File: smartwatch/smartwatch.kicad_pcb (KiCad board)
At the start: 2 copper layers, 40.1 x 40.1 mm, 2 parts, among them U1 ESP32-S3-WROOM-1, U2 AMS1117-3.3

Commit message: finished pcb and sch
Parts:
- added BOOT/FLASH1: BOOT/FLASH, Button_Switch_SMD:SW_SPST_Omron_B3FS-100xP, B.Cu at (72.2, 53.5)
- added C1: 10nF, Capacitor_SMD:C_0805_2012Metric_Pad1.18x1.45mm_HandSolder, B.Cu at (49.6, 71.7)
- added C10: 100nF, Capacitor_SMD:C_0805_2012Metric_Pad1.18x1.45mm_HandSolder, B.Cu at (58.2, 48.6)
- added C11: Polarized_10uF, Capacitor_Tantalum_SMD:CP_EIA-2012-12_Kemet-R_Pad1.30x1.05mm_HandSolder, B.Cu at (67.3, 71.8)
- added C12: Polarized_10uF, Capacitor_Tantalum_SMD:CP_EIA-2012-12_Kemet-R_Pad1.30x1.05mm_HandSolder, B.Cu at (57.1, 74.1)
- added C2: 100nF, Capacitor_SMD:C_0805_2012Metric_Pad1.18x1.45mm_HandSolder, B.Cu at (53.7, 71.6)
- added C3: 100nF, Capacitor_SMD:C_0805_2012Metric_Pad1.18x1.45mm_HandSolder, B.Cu at (44.8, 67.6)
- added C4: 10nF, Capacitor_SMD:C_0805_2012Metric_Pad1.18x1.45mm_HandSolder, B.Cu at (44.7, 64.3)
- added C5: 0.1uF, Capacitor_SMD:C_0805_2012Metric_Pad1.18x1.45mm_HandSolder, F.Cu at (45.6, 60.3)
- added C6: 2.2nF, Capacitor_SMD:C_0805_2012Metric_Pad1.18x1.45mm_HandSolder, F.Cu at (46.2, 52.3)
- added C7: 0.1uF, Capacitor_SMD:C_0805_2012Metric_Pad1.18x1.45mm_HandSolder, F.Cu at (41.7, 60.8)
- added C8: 10nF, Capacitor_SMD:C_0805_2012Metric_Pad1.18x1.45mm_HandSolder, F.Cu at (39.6, 56.6)
- added C9: 100nF, Capacitor_SMD:C_0805_2012Metric_Pad1.18x1.45mm_HandSolder, B.Cu at (72.2, 47.5)
- added GREEN1: CHARGED, LED_SMD:LED_0805_2012Metric_Pad1.15x1.40mm_HandSolder, B.Cu at (68.2, 60.2)
- added J1: BAT_CON, Connector_Wire_SMD:Wire_Pad_1x02, B.Cu at (64.1, 74.0)
- added J2: DC_CON, Connector_Wire_SMD:Wire_Pad_1x02, B.Cu at (59.6, 74.7)
- added J3: PROG_INT, Connector_Wire_SMD:Wire_Pad_1x02, F.Cu at (70.3, 52.3)
- added J4: I2C Touch, Connector_Wire_SMD:Wire_Pad_1x02, F.Cu at (75.4, 52.3)
- added J5: SPI Display, Connector_Wire_SMD:Wire_Pad_1x03, F.Cu at (70.1, 57.1)
- added J6: Power, Connector_Wire_SMD:Wire_Pad_1x02, B.Cu at (71.6, 67.6)
- added J7: Micro_SD_Card, Connector_Card:microSD_HC_Hirose_DM3D-SF, B.Cu at (49.3, 54.1)
- added R1: 2.2KΩ, Resistor_SMD:R_0805_2012Metric_Pad1.20x1.40mm_HandSolder, B.Cu at (63.6, 68.0)
- added R2: 470Ω, Resistor_SMD:R_0805_2012Metric_Pad1.20x1.40mm_HandSolder, B.Cu at (59.6, 60.3)
- added R3: 470Ω, Resistor_SMD:R_0805_2012Metric_Pad1.20x1.40mm_HandSolder, B.Cu at (68.0, 62.9)
- added RED1: CHARGING, LED_SMD:LED_0805_2012Metric_Pad1.15x1.40mm_HandSolder, B.Cu at (63.5, 60.3)
- added RST1: RST, Button_Switch_SMD:SW_SPST_Omron_B3FS-100xP, B.Cu at (61.8, 53.5)
- added U3: MPU-6050, Sensor_Motion:InvenSense_QFN-24_4x4mm_P0.5mm, F.Cu at (43.3, 56.2)
- added U4: TLV1117-33, Package_TO_SOT_SMD:SOT-223-3_TabPin2, B.Cu at (51.5, 66.3)
- U1: value ESP32-S3-WROOM-1 -> ESP32-WROVER-E
- U2: value AMS1117-3.3 -> MCP73831-5-OT; footprint Package_TO_SOT_SMD:SOT-223-3_TabPin2 -> Package_TO_SOT_SMD:SOT-23-5; moved to B.Cu
- moved U2 18.6 mm to (59.5, 68.1), turned to 180 degrees
- moved U1 0.29 mm to (58.6, 56.2)
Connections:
- U1 pad 1: Net-(U1-GND-Pad1) -> DC_GND
- U1 pad 13: unconnected-(U1-GPIO19/U1RTS/ADC2_CH8/CLK_OUT2/USB_D--Pad13) -> SD_SCLK
- U1 pad 14: unconnected-(U1-GPIO20/U1CTS/ADC2_CH9/CLK_OUT1/USB_D+-Pad14) -> SD_MISO
- U1 pad 15: unconnected-(U1-GPIO3/TOUCH3/ADC1_CH2-Pad15) -> DC_GND
- U1 pad 16: unconnected-(U1-GPIO46-Pad16) -> SD_MOSI
- U1 pad 17: unconnected-(U1-GPIO9/TOUCH9/ADC1_CH8/FSPIHD/SUBSPIHD-Pad17) -> (no net)
- U1 pad 18: unconnected-(U1-GPIO10/TOUCH10/ADC1_CH9/FSPICS0/FSPIIO4/SUBSPICS0-Pad18) -> (no net)
- U1 pad 19: unconnected-(U1-GPIO11/TOUCH11/ADC2_CH0/FSPID/FSPIIO5/SUBSPID-Pad19) -> (no net)
- U1 pad 2: unconnected-(U1-3V3-Pad2) -> 3V3
- U1 pad 20: unconnected-(U1-GPIO12/TOUCH12/ADC2_CH1/FSPICLK/FSPIIO6/SUBSPICLK-Pad20) -> (no net)
- U1 pad 21: unconnected-(U1-GPIO13/TOUCH13/ADC2_CH2/FSPIQ/FSPIIO7/SUBSPIQ-Pad21) -> (no net)
- U1 pad 22: unconnected-(U1-GPIO14/TOUCH14/ADC2_CH3/FSPIWP/FSPIDQS/SUBSPIWP-Pad22) -> (no net)
- U1 pad 23: unconnected-(U1-GPIO21-Pad23) -> SD_SS
- U1 pad 24: unconnected-(U1-GPIO47/SPICLK_P/SUBSPICLK_P_DIFF-Pad24) -> IO2
- U1 pad 25: unconnected-(U1-GPIO48/SPICLK_N/SUBSPICLK_N_DIFF-Pad25) -> IO0
- U1 pad 27: unconnected-(U1-GPIO0/BOOT-Pad27) -> (no net)
- U1 pad 28: unconnected-(U1-SPIIO6/GPIO35/FSPID/SUBSPID-Pad28) -> (no net)
- U1 pad 3: unconnected-(U1-EN-Pad3) -> EN
- U1 pad 30: unconnected-(U1-SPIDQS/GPIO37/FSPIQ/SUBSPIQ-Pad30) -> SCR_SCLK
- U1 pad 31: unconnected-(U1-GPIO38/FSPIWP/SUBSPIWP-Pad31) -> SCR_MISO
- U1 pad 32: unconnected-(U1-MTCK/GPIO39/CLK_OUT3/SUBSPICS1-Pad32) -> (no net)
- U1 pad 33: unconnected-(U1-MTDO/GPIO40/CLK_OUT2-Pad33) -> TOUCH_SDA
- U1 pad 34: unconnected-(U1-MTDI/GPIO41/CLK_OUT1-Pad34) -> RX
- U1 pad 35: unconnected-(U1-MTMS/GPIO42-Pad35) -> TX
- U1 pad 36: unconnected-(U1-U0RXD/GPIO44/CLK_OUT2-Pad36) -> TOUCH_SCL
- U1 pad 37: unconnected-(U1-U0TXD/GPIO43/CLK_OUT1-Pad37) -> SCR_MOSI
- U1 pad 38: unconnected-(U1-GPIO2/TOUCH2/ADC1_CH1-Pad38) -> DC_GND
- U1 pad 39: unconnected-(U1-GPIO1/TOUCH1/ADC1_CH0-Pad39) -> DC_GND
- U1 pad 8: unconnected-(U1-GPIO15/U0RTS/ADC2_CH4/XTAL_32K_P-Pad8) -> MPU_SDA
- U1 pad 9: unconnected-(U1-GPIO16/U0CTS/ADC2_CH5/XTAL_32K_N-Pad9) -> MPU_SCL
- U2 pad 1: unconnected-(U2-GND-Pad1) -> MCP_1
- U2 pad 2: unconnected-(U2-VO-Pad2) -> DC_GND
- U2 pad 3: unconnected-(U2-VI-Pad3) -> BAT_VDD
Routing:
- net DC_GND: track 0.00 -> 192.3 mm, vias 0 -> 12
- net 3V3: track 0.00 -> 71.5 mm, vias 0 -> 5
- net SD_SS: track 0.00 -> 29.6 mm, vias 0 -> 2
- net BAT_VDD: track 0.00 -> 26.9 mm, vias 0 -> 3
- net IO0: track 0.00 -> 25.4 mm, vias 0 -> 2
- net EN: track 0.00 -> 19.1 mm, vias 0 -> 1
- net DC_5V_IN: track 0.00 -> 17.7 mm
- net SD_MOSI: track 0.00 -> 16.7 mm, vias 0 -> 2
- net MPU_SDA: track 0.00 -> 13.1 mm, vias 0 -> 2
- net MPU_SCL: track 0.00 -> 12.2 mm, vias 0 -> 2
- net SD_SCLK: track 0.00 -> 12.0 mm, vias 0 -> 1
- net SD_MISO: track 0.00 -> 11.4 mm, vias 0 -> 2
- net MCP_1: track 0.00 -> 11.2 mm
- net SCR_MOSI: track 0.00 -> 11.0 mm, vias 0 -> 2
- net TOUCH_SDA: track 0.00 -> 8.52 mm
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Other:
- copper layers 2 -> 4
- board text added: "3V3"
- board text added: "DCIN"
- board text added: "GND"
- board text added: "MISO"
- board text added: "MOSI"
- board text added: "RX"
- board text added: "SCLK"
- board text added: "SCR"
- board text added: "TX"
- board text added: "T_SCL"
- board text added: "T_SDA"
- board text added: "VDD"

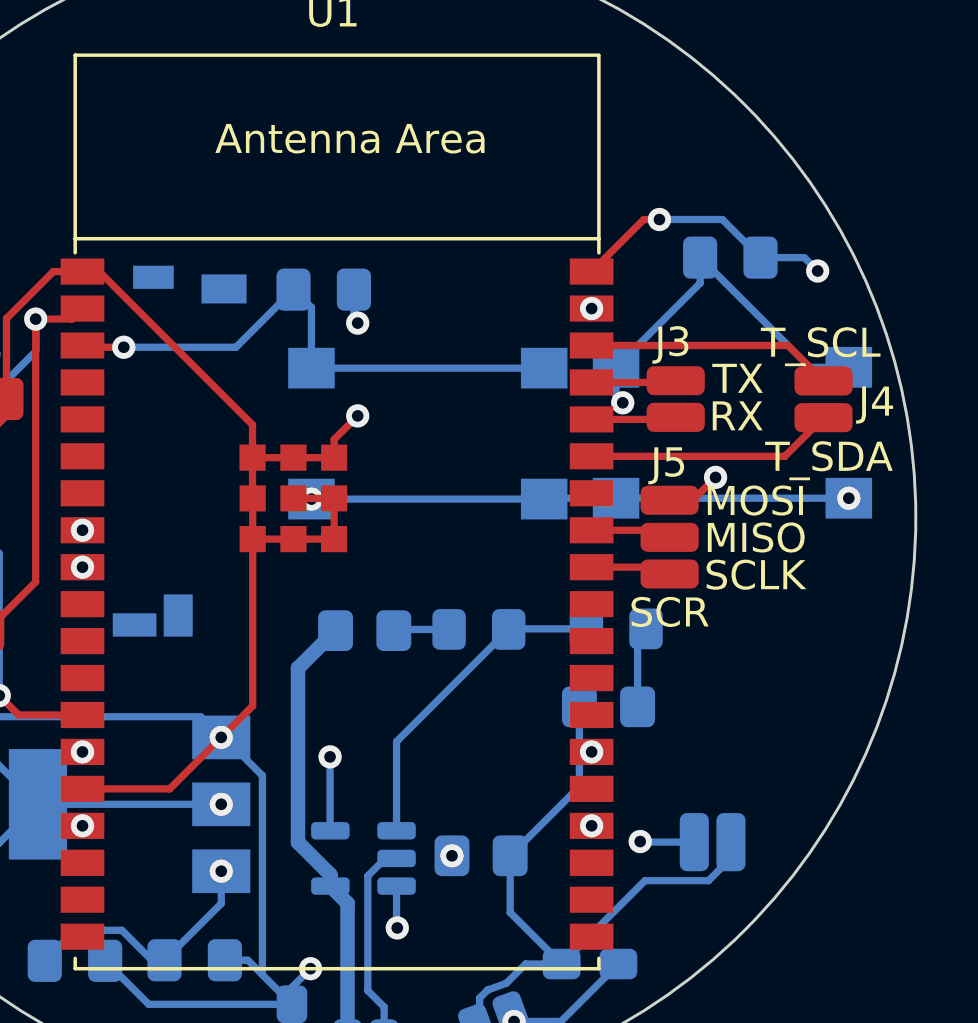
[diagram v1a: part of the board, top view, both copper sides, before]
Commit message: added button
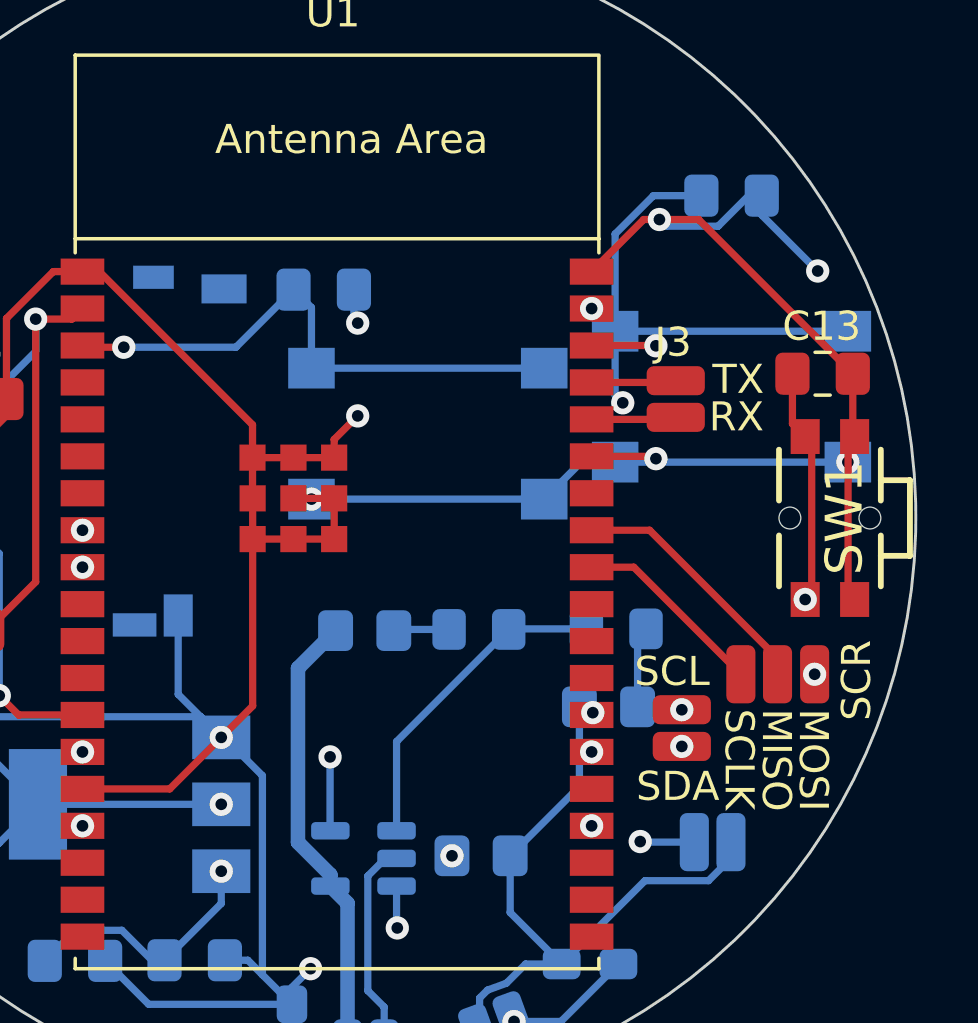
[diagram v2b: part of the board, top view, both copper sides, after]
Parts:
- added C13: 100nF, Capacitor_SMD:C_0805_2012Metric_Pad1.18x1.45mm_HandSolder, F.Cu at (75.3, 51.5)
- added SW1: SW_Push, Side_Button:Wurth_Elektronik_436331045822, F.Cu at (76.1, 56.4)
- moved J4 12.3 mm to (70.5, 63.6)
- moved J5 5.99 mm to (73.8, 61.8), turned to 0 degrees
- moved C9 2.13 mm to (72.2, 45.4)
- moved BOOT/FLASH1 1.24 mm to (72.2, 52.3)
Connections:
- J7 pad 9: unconnected-(J7-SHIELD-Pad9) -> DC_GND
- U1 pad 26: unconnected-(U1-ADC2_CH0/GPIO4-Pad26) -> BTN_INP
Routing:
- net DC_GND: track 192.3 -> 214.4 mm
- net BTN_INP: track 0.00 -> 17.1 mm, vias 0 -> 2
- net TOUCH_SCL: track 8.48 -> 15.5 mm, vias 0 -> 2
- net SCR_MOSI: track 11.0 -> 17.3 mm
- net SCR_MISO: track 2.78 -> 8.76 mm
- net IO0: track 25.4 -> 29.9 mm
- net TOUCH_SDA: track 8.52 -> 12.5 mm, vias 0 -> 2
- net SCR_SCLK: track 2.78 -> 6.65 mm
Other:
- board text added: "SCL"
- board text added: "SDA"
- board text removed: "T_SCL"
- board text removed: "T_SDA"

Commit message: updated pcb schematic and design
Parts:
- removed J7: Micro_SD_Card, Connector_Card:microSD_HC_Hirose_DM3D-SF
- added J8: SD Card, Connector_Wire_SMD:Wire_Pad_1x06, B.Cu at (33.3, 46.2)
- J4: value I2C Touch -> Screen; footprint Connector_Wire_SMD:Wire_Pad_1x02 -> Connector_Wire_SMD:Wire_Pad_1x07
- J5: value SPI Display -> Touch; footprint Connector_Wire_SMD:Wire_Pad_1x03 -> Connector_Wire_SMD:Wire_Pad_1x04
- J6: moved to F.Cu
- moved RST1 33.3 mm to (33.1, 36.5)
- moved GREEN1 31.2 mm to (41.1, 44.8)
- moved J5 29.5 mm to (57.7, 37.0), turned to -90 degrees
- moved R1 29.0 mm to (38.9, 52.8), turned to 180 degrees
- moved R3 28.7 mm to (45.8, 44.7), turned to 0 degrees
- moved C5 27.5 mm to (31.8, 36.5), turned to -90 degrees
- moved RED1 25.5 mm to (41.1, 48.2)
- moved C12 24.3 mm to (38.2, 58.9), turned to 0 degrees
- moved C11 23.7 mm to (49.5, 56.1), turned to -90 degrees
- moved C6 23.4 mm to (28.1, 37.6), turned to 90 degrees
- moved C9 22.3 mm to (51.6, 36.7), turned to 90 degrees
- moved C10 22.3 mm to (39.4, 36.6), turned to 90 degrees
- moved J4 22.2 mm to (57.6, 45.5)
- moved J2 22.1 mm to (42.6, 60.7)
- moved BOOT/FLASH1 21.2 mm to (57.9, 36.6)
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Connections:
- J4 pad 1: TOUCH_SCL -> SCR_MISO
- J4 pad 2: TOUCH_SDA -> SCR_MOSI
- J5 pad 1: SCR_SCLK -> TOUCH_RST
- J5 pad 2: SCR_MISO -> TOUCH_IRQ
- J5 pad 3: SCR_MOSI -> TOUCH_SCL
- U1 pad 10: unconnected-(U1-DAC_1/ADC2_CH8/GPIO25-Pad10) -> TOUCH_IRQ
- U1 pad 11: unconnected-(U1-DAC_2/ADC2_CH9/GPIO26-Pad11) -> TOUCH_RST
- U1 pad 12: unconnected-(U1-ADC2_CH7/GPIO27-Pad12) -> SD_SS
- U1 pad 23: SD_SS -> SCR_RST
- U1 pad 26: BTN_INP -> unconnected-(U1-ADC2_CH0/GPIO4-Pad26)
- U1 pad 29: unconnected-(U1-GPIO5-Pad29) -> SCR_CS
- U1 pad 31: SCR_MISO -> SCR_DC
- U1 pad 6: unconnected-(U1-GPIO34/ADC1_CH6-Pad6) -> BTN_INP
- U1 pad 7: unconnected-(U1-GPIO35/ADC1_CH7-Pad7) -> SCR_MISO
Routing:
- net TOUCH_RST: track 0.00 -> 27.2 mm, vias 0 -> 2
- net SD_SS: track 29.6 -> 3.15 mm, vias 2 -> 1
- net TOUCH_IRQ: track 0.00 -> 25.6 mm, vias 0 -> 3
- net BTN_INP: track 17.1 -> 34.2 mm
- net 3V3: track 71.5 -> 57.3 mm, vias 5 -> 3
- net SCR_MISO: track 8.76 -> 21.9 mm, vias 0 -> 2
- net SD_MOSI: track 16.7 -> 6.04 mm
- net TOUCH_SCL: track 15.5 -> 4.85 mm, vias 2 -> 0
- net SCR_RST: track 0.00 -> 7.67 mm
- net TOUCH_SDA: track 12.5 -> 4.94 mm, vias 2 -> 0
- net SCR_MOSI: track 17.3 -> 10.0 mm
- net TX: track 2.91 -> 10.1 mm, vias 0 -> 2
- net RX: track 2.92 -> 10.1 mm, vias 0 -> 2
- net SCR_DC: track 0.00 -> 5.91 mm, vias 0 -> 2
- net BAT_VDD: track 26.9 -> 21.5 mm
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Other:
- board text removed: "3V3"
- board text removed: "DCIN"
- board text removed: "GND"
- board text removed: "MISO"
- board text removed: "MOSI"
- board text removed: "RX"
- board text removed: "SCL"
- board text removed: "SCLK"
- board text removed: "SCR"
- board text removed: "SDA"
- board text removed: "TX"
- board text removed: "VDD"

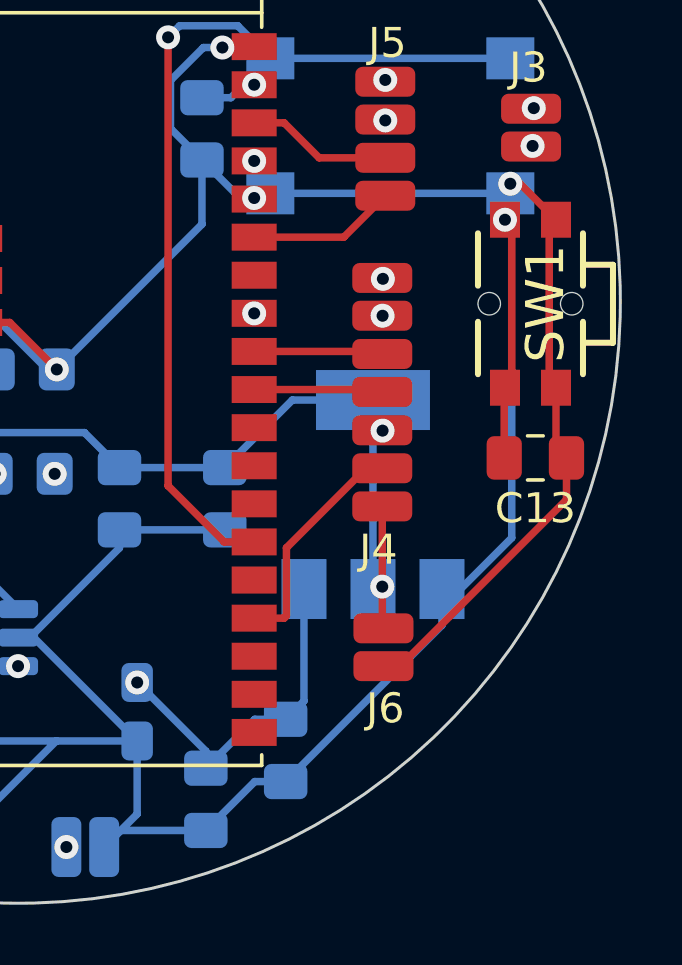
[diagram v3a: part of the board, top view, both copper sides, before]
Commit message: changed schematic and pcb of push button connection
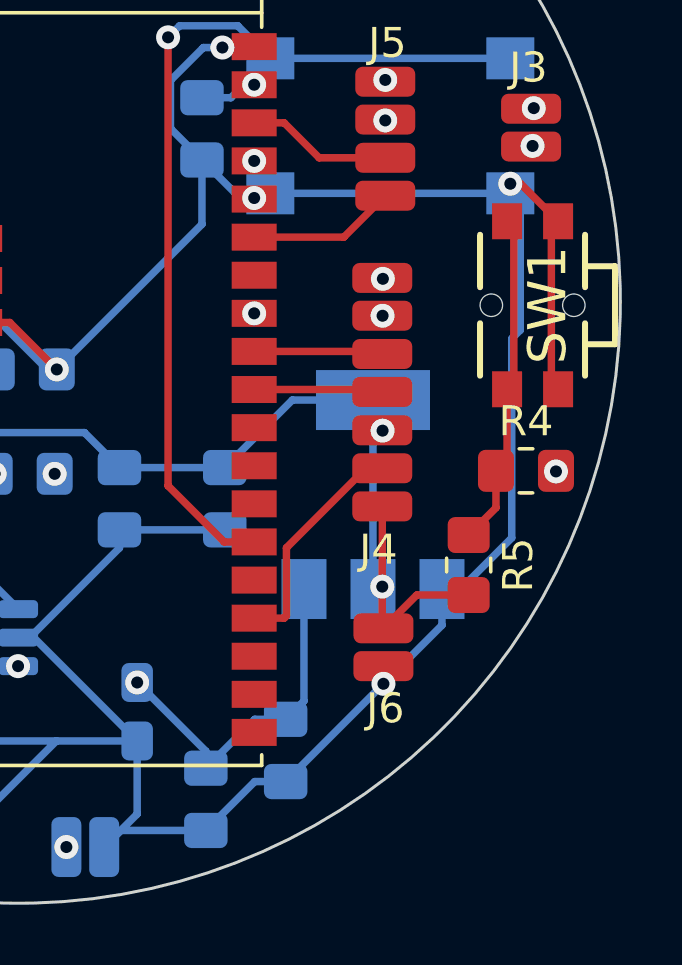
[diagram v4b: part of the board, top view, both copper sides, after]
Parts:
- removed C13: 100nF, Capacitor_SMD:C_0805_2012Metric_Pad1.18x1.45mm_HandSolder
- added R4: 10KΩ, Resistor_SMD:R_0805_2012Metric_Pad1.20x1.40mm_HandSolder, F.Cu at (62.4, 48.1)
- added R5: 10KΩ, Resistor_SMD:R_0805_2012Metric_Pad1.20x1.40mm_HandSolder, F.Cu at (60.5, 51.2)
- moved SW1 0.09 mm to (63.1, 42.6)
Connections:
- SW1 pad 1: BTN_INP -> Net-(R4-Pad1)
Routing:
- net DC_GND: track 211.9 -> 200.6 mm, vias 4 -> 5
- net Net-(R4-Pad1): track 0.00 -> 11.2 mm
- net 3V3: track 57.3 -> 60.6 mm

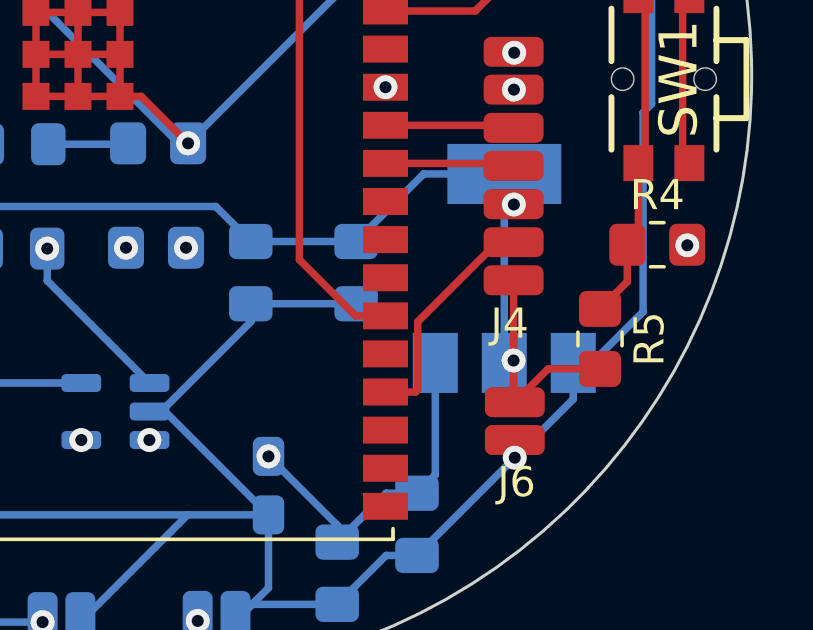
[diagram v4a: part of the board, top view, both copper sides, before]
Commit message: backlight toggling, stepcount ring
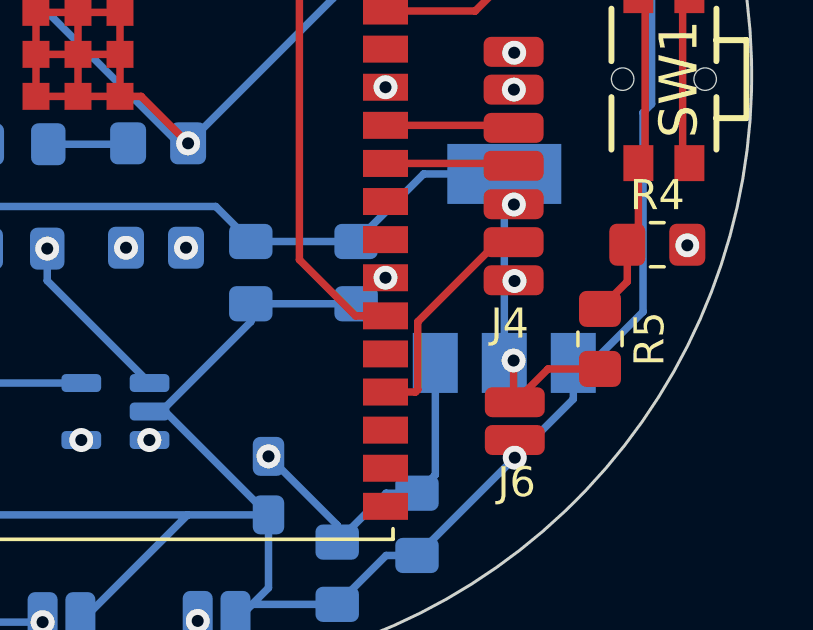
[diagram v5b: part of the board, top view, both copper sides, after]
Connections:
- J4 pad 7: 3V3 -> SCR_BL
- U1 pad 26: unconnected-(U1-ADC2_CH0/GPIO4-Pad26) -> SCR_BL
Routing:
- net SCR_BL: track 0.00 -> 4.39 mm, vias 0 -> 2
- net 3V3: track 60.6 -> 57.9 mm
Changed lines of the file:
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@@
   (net 33 "TOUCH_RST")
   (net 34 "TOUCH_IRQ")
-  (net 35 "unconnected-(U1-ADC2_CH0{slash}GPIO4-Pad26)")
+  (net 35 "SCR_BL")
   (net 36 "IO2")
   (net 37 "unconnected-(U3-NC-Pad2)")
@@
       (net 1 "IO0") (pinfunction "GPIO0/BOOT/ADC2_CH1") (pintype "bidirectional"))
     (pad "26" smd rect (at 8.75 6.985) (size 1.5 0.9) (layers "F.Cu" "F.Paste" "F.Mask")
-      (net 35 "unconnected-(U1-ADC2_CH0{slash}GPIO4-Pad26)") (pinfunction "ADC2_CH0/GPIO4") (pintype "bidirectional"))
+      (net 35 "SCR_BL") (pinfunction "ADC2_CH0/GPIO4") (pintype "bidirectional"))
     (pad "27" smd rect (at 8.75 5.715) (size 1.5 0.9) (layers "F.Cu" "F.Paste" "F.Mask"))
     (pad "28" smd rect (at 8.75 4.445) (size 1.5 0.9) (layers "F.Cu" "F.Paste" "F.Mask"))
@@
       (net 30 "SCR_RST") (pinfunction "Pin_6") (pintype "passive"))
     (pad "7" smd roundrect (at 3.805 0 270) (size 1 2) (layers "F.Cu" "F.Paste" "F.Mask") (roundrect_rratio 0.25)
-      (net 4 "3V3") (pinfunction "Pin_7") (pintype "passive"))
+      (net 35 "SCR_BL") (pinfunction "Pin_7") (pintype "passive"))
   )
   (footprint "Capacitor_SMD:C_0805_2012Metric_Pad1.18x1.45mm_HandSolder" (layer "F.Cu")
@@
   (segment (start 58.79 52.25) (end 57.68 53.36) (width 0.25) (layer "F.Cu") (net 4))
   (segment (start 31.82 35.4625) (end 32.87 36.5125) (width 0.25) (layer "F.Cu") (net 4))
-  (segment (start 57.64 49.295) (end 57.64 51.97) (width 0.25) (layer "F.Cu") (net 4))
   (segment (start 57.64 51.97) (end 57.64 53.32) (width 0.25) (layer "F.Cu") (net 4))
   (segment (start 32.0425 35.24) (end 31.82 35.4625) (width 0.25) (layer "F.Cu") (net 4))
@@
   (segment (start 57.74 36.43) (end 49.68 36.43) (width 0.25) (layer "In2.Cu") (net 34))
   (segment (start 49.68 36.43) (end 49.65 36.46) (width 0.25) (layer "In2.Cu") (net 34))
+  (segment (start 57.645 49.295) (end 57.67 49.32) (width 0.25) (layer "F.Cu") (net 35))
+  (segment (start 57.64 49.295) (end 57.645 49.295) (width 0.25) (layer "F.Cu") (net 35))
+  (via blind (at 53.37 49.21) (size 0.8) (drill 0.4) (layers "F.Cu" "In1.Cu") (net 35))
+  (via blind (at 57.67 49.32) (size 0.8) (drill 0.4) (layers "F.Cu" "In1.Cu") (net 35))
+  (segment (start 53.48 49.32) (end 53.37 49.21) (width 0.25) (layer "In1.Cu") (net 35))
+  (segment (start 57.67 49.32) (end 53.48 49.32) (width 0.25) (layer "In1.Cu") (net 35))
   (segment (start 61.8 39.79) (end 62.025 40.015) (width 0.25) (layer "F.Cu") (net 52))
   (segment (start 61.43 48.11) (end 61.43 49.34) (width 0.25) (layer "F.Cu") (net 52))
